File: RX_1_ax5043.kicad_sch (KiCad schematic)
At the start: 22 parts, among them J6 2118714-2, P5 CONUFL001-SMD-T, U21 AX5043, U22 TPS22929D

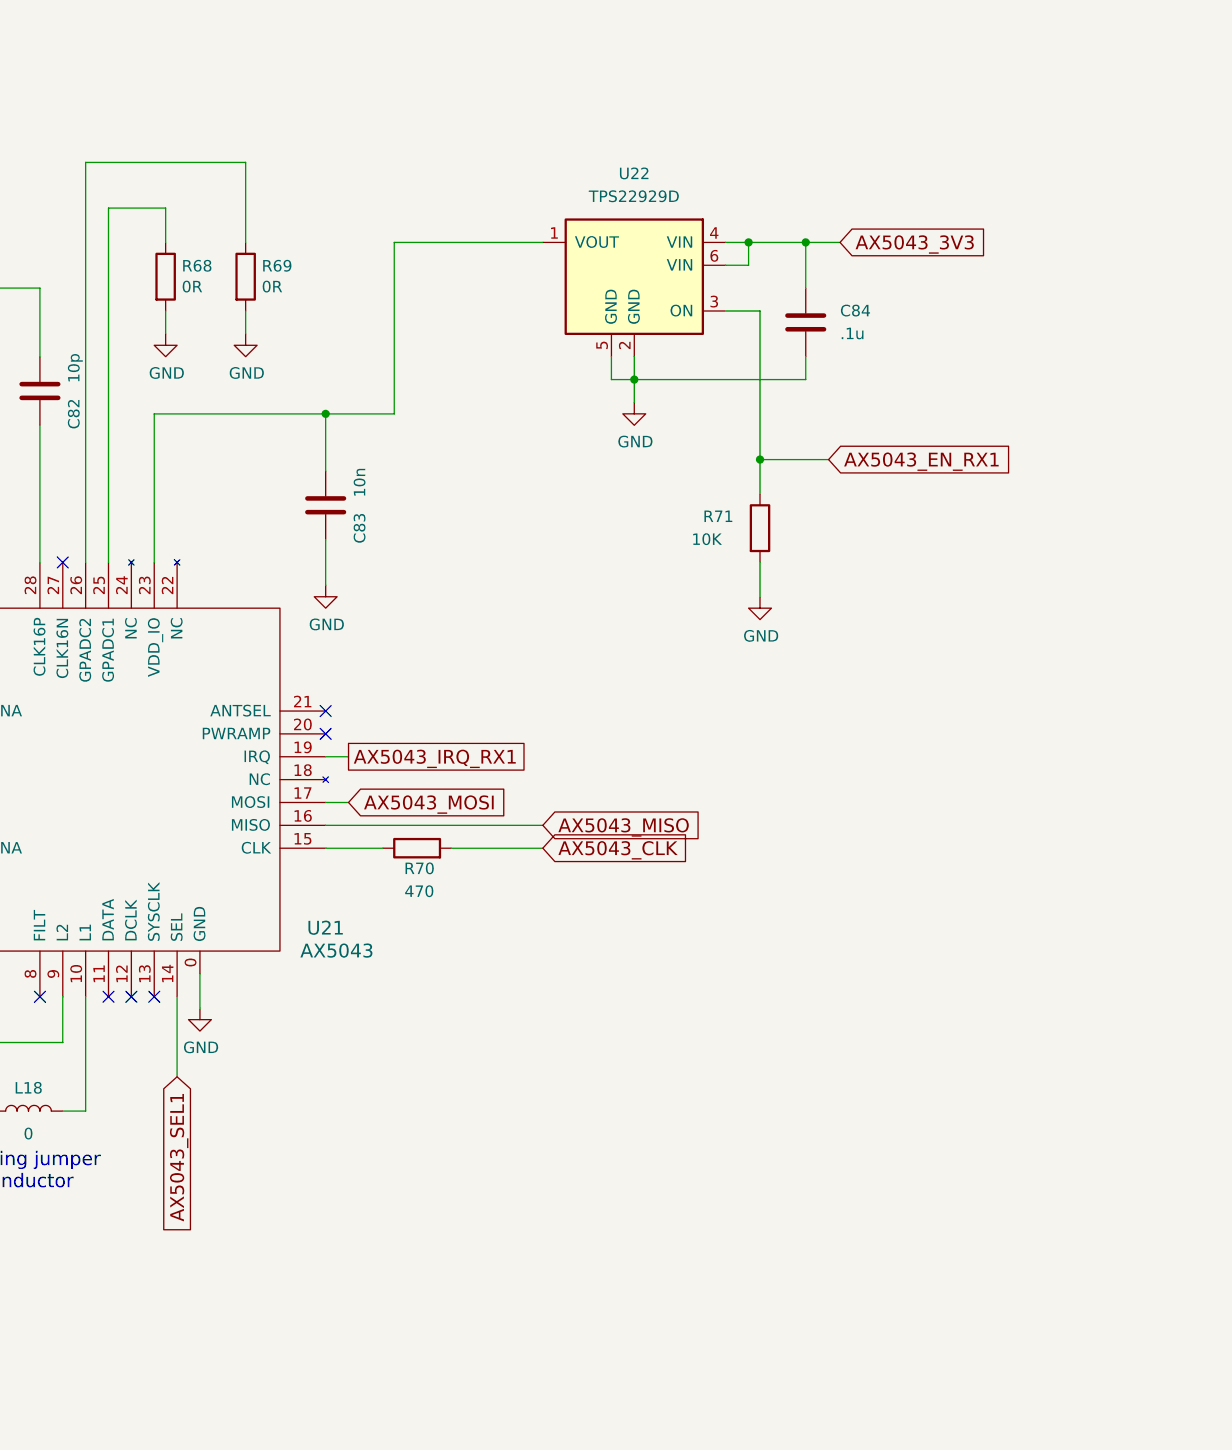
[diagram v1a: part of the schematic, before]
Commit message: Replace AX5043 power controls with MOSFETs
They are simpler, use less power, and are more reliable.

Signed-off-by: Corey Minyard <corey@minyard.net>
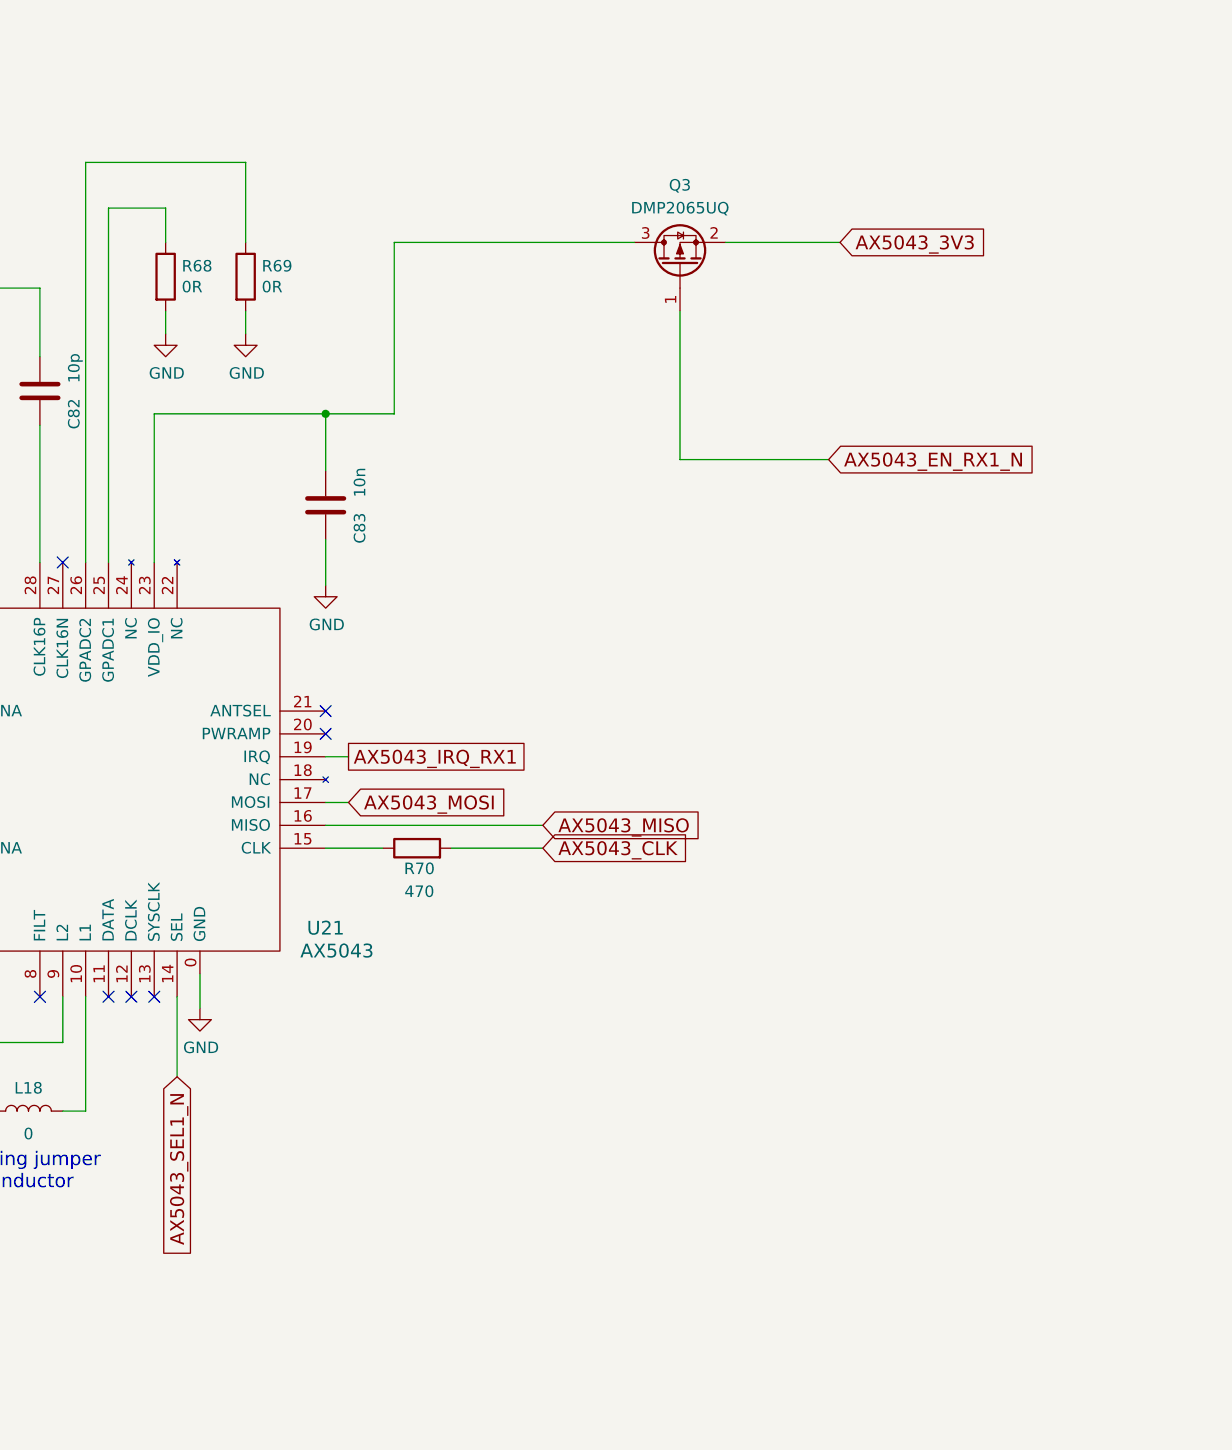
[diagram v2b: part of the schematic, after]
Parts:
- removed C84: .1u, Capacitor_SMD:C_0603_1608Metric_Pad1.08x0.95mm_HandSolder, symbol Device:C
- removed R71: 10K, Resistor_SMD:R_0603_1608Metric_Pad0.98x0.95mm_HandSolder, symbol Device:R
- removed U22: TPS22929D, Package_TO_SOT_SMD:SOT-23-6, symbol Power_Management:TPS22929D
- added Q3: DMP2065UQ, Package_TO_SOT_SMD:SOT-23, symbol Transistor_FET:Q_PMOS_GSD
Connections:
- net AX5043_3V3: now also Q3.2 (S)
- net at C83.1, U21.23 (VDD_IO): now also Q3.3 (D)
- net AX5043_SEL1 renamed AX5043_SEL1_N
- new net AX5043_EN_RX1_N: Q3.1 (G)

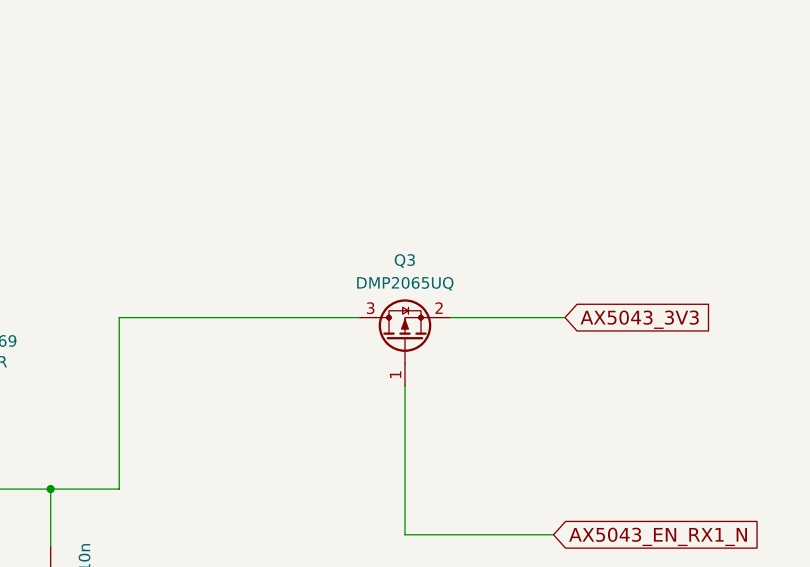
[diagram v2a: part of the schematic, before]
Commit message: Replace the AX5043 MOSFETs again
A little wider VTgs and lower on resistance.

Signed-off-by: Corey Minyard <corey@minyard.net>
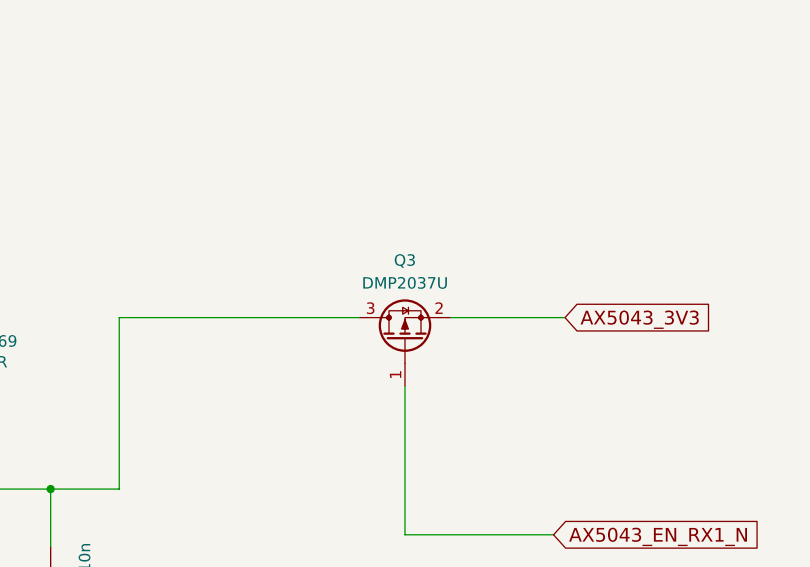
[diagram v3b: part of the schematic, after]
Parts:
- Q3: value DMP2065UQ -> DMP2037U
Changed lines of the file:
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@@
 			)
 		)
-		(property "Value" "DMP2065UQ"
+		(property "Value" "DMP2037U"
 			(at 284.48 72.39 90)
 			(effects

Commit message: Check over notes and some component values
Fix a wrong capacitor in one spot, set Q and voltage as necessary.

Signed-off-by: Corey Minyard <corey@minyard.net>
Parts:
- L15, L16: value 78n -> 78n 2% Q=28
- L17: value 1n -> 1n Q=12
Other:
- note added: "All RF capacitors C0G/NP0."
- note removed: "Inductors Ref Murata LQW18AN_00 series"
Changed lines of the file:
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@@
 		(comment 1 "N5BRG")
-	)
-	(text "Inductors Ref Murata LQW18AN_00 series"
-		(exclude_from_sim no)
-		(at 83.185 182.88 0)
-		(effects
-			(font
-				(size 1.524 1.524)
-			)
-			(justify left bottom)
-		)
 	)
 	(text "RECEIVER 1"
@@
 				(size 1.524 1.524)
 			)
+		)
+	)
+	(text "All RF capacitors C0G/NP0."
+		(exclude_from_sim no)
+		(at 135.636 177.292 0)
+		(effects
+			(font
+				(size 1.524 1.524)
+			)
+			(justify left bottom)
 		)
 	)
@@
 			)
 		)
-		(property "Value" "1n"
+		(property "Value" "1n Q=12"
 			(at 175.514 145.796 90)
 			(effects
@@
 			)
 		)
-		(property "Value" "78n"
+		(property "Value" "78n 2% Q=28"
 			(at 143.51 131.572 90)
 			(effects
@@
 			)
 		)
-		(property "Value" "78n"
+		(property "Value" "78n 2% Q=28"
 			(at 165.608 146.05 90)
 			(effects

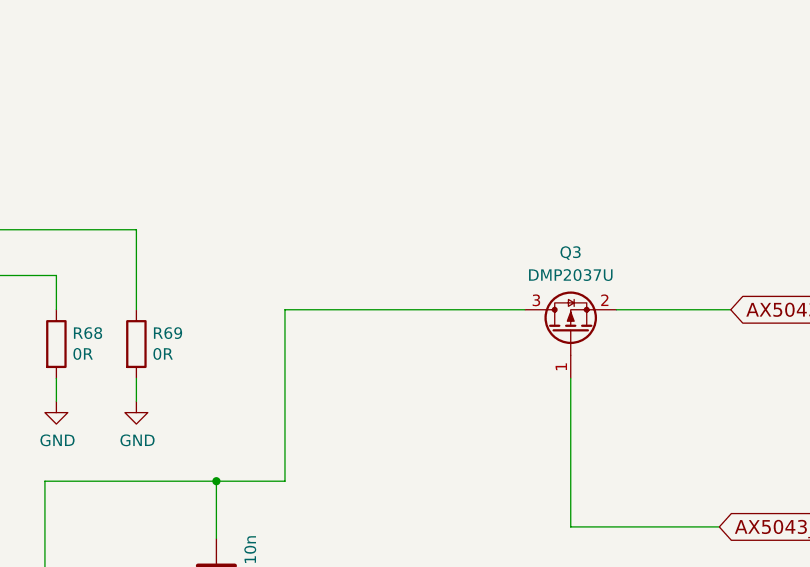
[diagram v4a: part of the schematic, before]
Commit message: Add ferrite beads to the AX5043s' power inputs
Signed-off-by: Corey Minyard <corey@minyard.net>
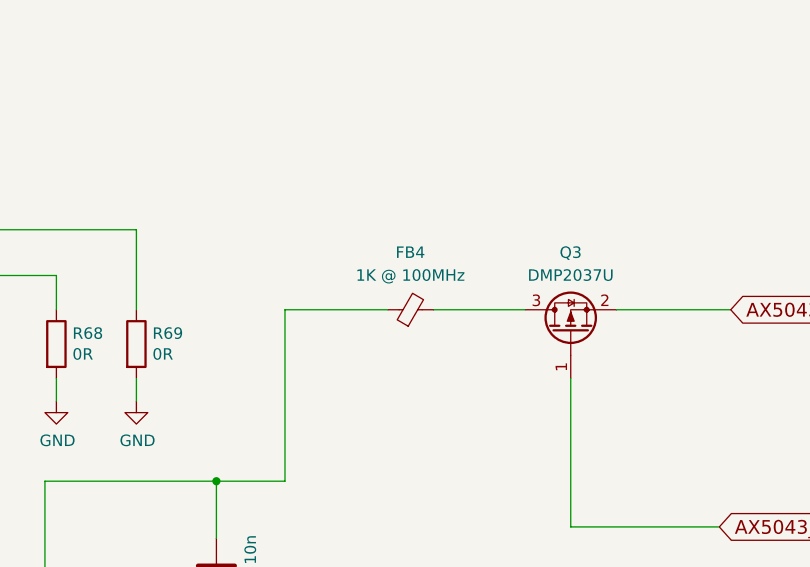
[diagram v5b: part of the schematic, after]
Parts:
- added FB4: 1K @ 100MHz, Resistor_SMD:R_0603_1608Metric_Pad0.98x0.95mm_HandSolder, symbol Device:FerriteBead_Small
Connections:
- net at C83.1, U21.23 (VDD_IO): now also FB4.1; no longer Q3.3 (D)
- new net: FB4.2, Q3.3 (D)
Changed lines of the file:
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@@
 	(wire
 		(pts
-			(xy 252.73 76.2) (xy 279.4 76.2)
+			(xy 252.73 76.2) (xy 264.16 76.2)
 		)
 		(stroke
@@
 		(pts
 			(xy 227.33 72.39) (xy 227.33 76.2)
+		)
+		(stroke
+			(width 0)
+			(type default)
+		)
+	)
+	(wire
+		(pts
+			(xy 269.24 76.2) (xy 279.4 76.2)
 		)
 		(stroke
@@
 					(unit 1)
 				)
+			)
+		)
+	)
+	(symbol
+		(lib_id "Device:FerriteBead_Small")
+		(at 266.7 76.2 90)
+		(unit 1)
+		(exclude_from_sim no)
+		(in_bom yes)
+		(on_board yes)
+		(dnp no)
+		(fields_autoplaced yes)
+		(property "Reference" "FB4"
+			(at 266.6619 69.85 90)
+			(effects
+				(font
+					(size 1.27 1.27)
+				)
+			)
+		)
+		(property "Value" "1K @ 100MHz"
+			(at 266.6619 72.39 90)
+			(effects
+				(font
+					(size 1.27 1.27)
+				)
+			)
+		)
+		(property "Footprint" "Resistor_SMD:R_0603_1608Metric_Pad0.98x0.95mm_HandSolder"
+			(at 266.7 77.978 90)
+			(effects
+				(font
+					(size 1.27 1.27)
+				)
+				(hide yes)
+			)
+		)
+		(property "Datasheet" "~"
+			(at 266.7 76.2 0)
+			(effects
+				(font
+					(size 1.27 1.27)
+				)
+				(hide yes)
+			)
+		)
+		(property "Description" "FerriteBead_Small"
+			(at 266.7 76.2 0)
+			(effects
+				(font
+					(size 1.27 1.27)
+				)
+				(hide yes)
+			)
+		)
+		(pin "1"
+		)
+		(pin "2"
+		)
+		(instances
+			(project "PacSat_AFSK"
+				(path "/cc9f42d2-6985-41ac-acab-5ab7b01c5b38/d9a83ee4-3280-49b9-88b8-54d26cbd8ed1/bc27fde3-8cca-4897-854d-674b6eeb65de"
+					(reference "FB4")
+					(unit 1)
+				)
